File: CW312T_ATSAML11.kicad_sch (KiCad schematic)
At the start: 12 parts, among them P1 PCIEx4 EDGE CONNECTOR, U1 ATSMAL11E16A-AU

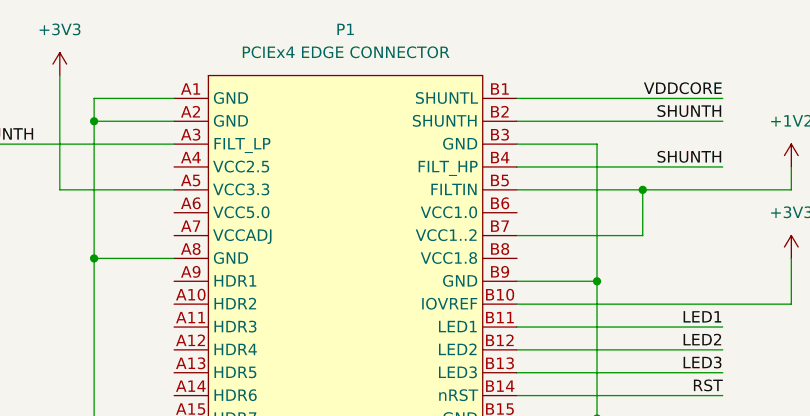
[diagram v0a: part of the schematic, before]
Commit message: updated pcb based off feedback
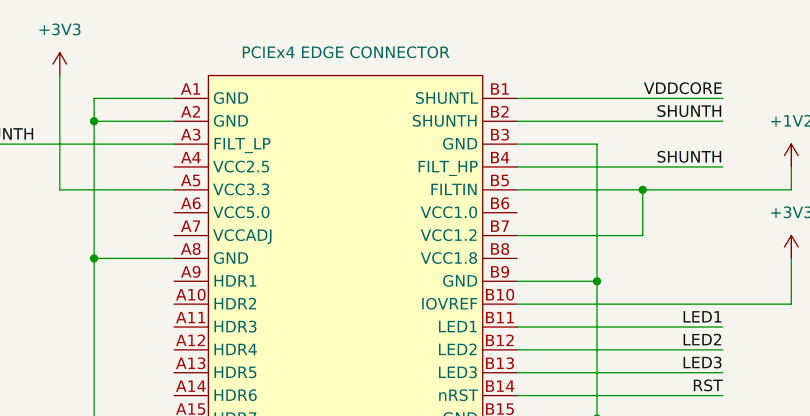
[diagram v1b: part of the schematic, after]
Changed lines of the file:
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@@
 					(size 1.27 1.27)
 				)
+				(hide yes)
 			)
 		)

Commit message: updated ATSAML11 design - Ready for Review
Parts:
- added PCB1: CE, Silkscrren_Symbols:CE-Logo_8.5x6mm_SilkScreen, symbol Silkscreen_Symbols:CE_Free
- added PCB2: Pb_Free, Silkscrren_Symbols:Pb_Free_8.0x8.0mm_SilkScreen, symbol Silkscreen_Symbols:Pb_Free
- added PCB3: WEEE, Silkscrren_Symbols:WEEE-Logo_5.6x8mm_SilkScreen, symbol Silkscreen_Symbols:WEEE
- renumbered C7 to C5, C8 to C6, C5 to C7
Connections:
- no-connect marks 0 -> 46

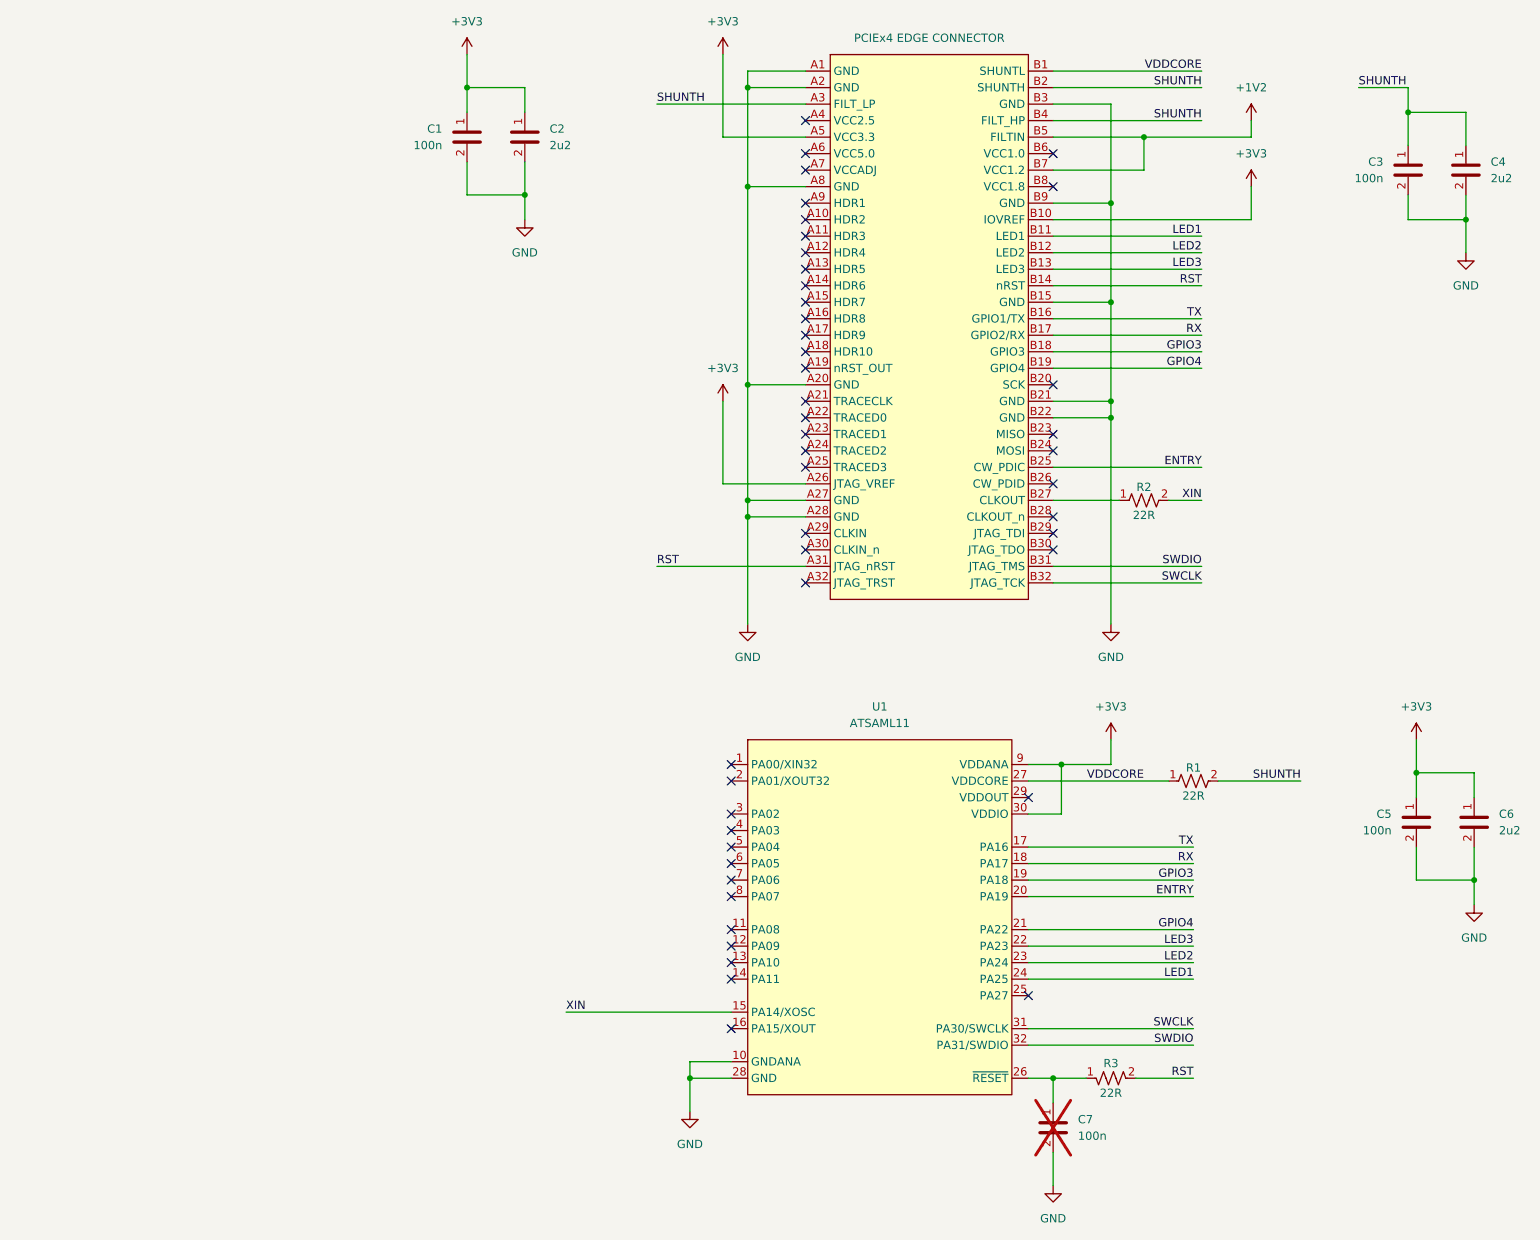
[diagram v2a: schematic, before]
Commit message: updated design -removed pin numbers from passives, updated cap placement, updated silkscreen
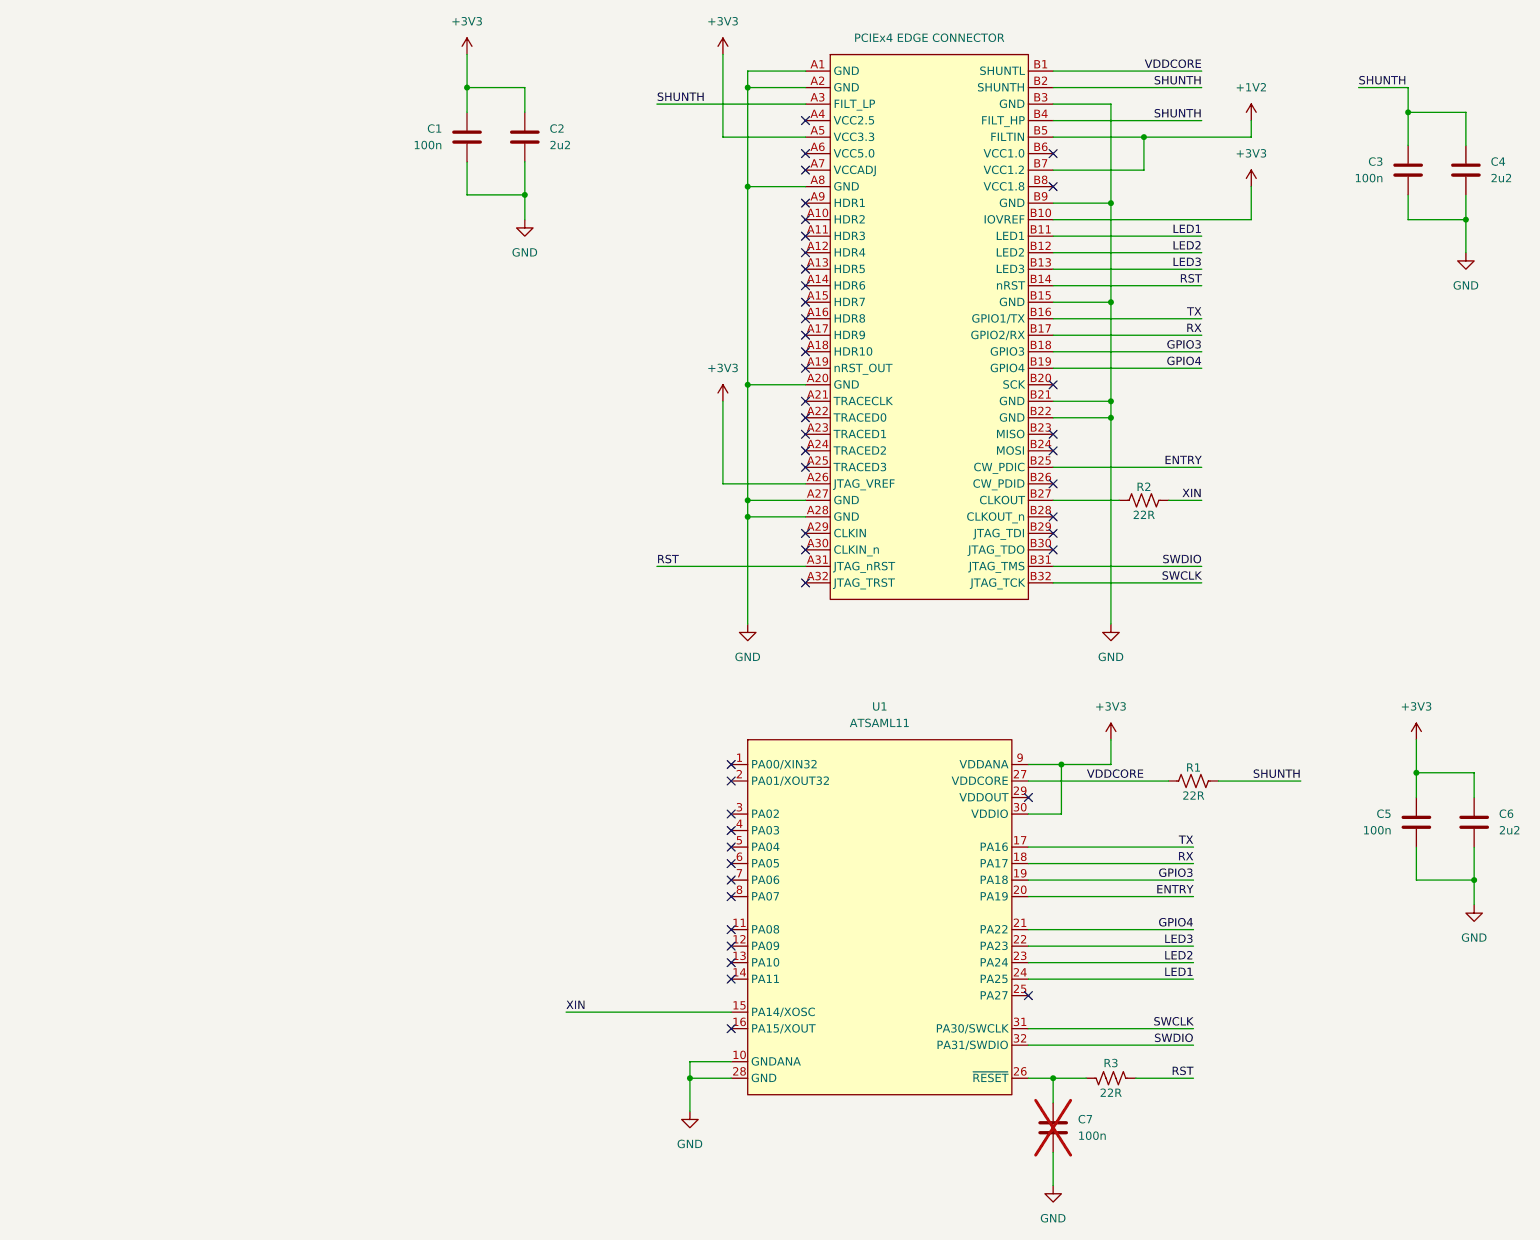
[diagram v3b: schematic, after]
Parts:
- added PCB4: UKCA symbol, Silkscrren_Symbols:UKCA-Logo_8x8mm_SilkScreen, symbol Silkscreen_Symbols:UKCA
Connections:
- net +3V3: now also C1., C2., C5., C6.; no longer C1.1, C2.1, C5.1, C6.1
- net GND: now also C1., C2., C3., C4., C5., C6., C7.; no longer C1.2, C2.2, C3.2, C4.2, C5.2, C6.2, C7.2
- net RST: now also R3.; no longer R3.2
- net SHUNTH: now also C3., C4., R1.; no longer C3.1, C4.1, R1.2
- net VDDCORE: now also R1.; no longer R1.1
- net XIN: now also R2.; no longer R2.2
- net at P1.B27 (CLKOUT): now also R2.; no longer R2.1
- new net: C7., R3., U1.26 (~{RESET})
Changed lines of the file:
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@@
 	)
 	(symbol
+		(lib_name "tutorial_2_library:CAP_100n_50V_0603")
 		(lib_id "tutorial_2_library:CAP_100n_50V_0603")
 		(at 181.61 140.97 90)
@@
 			)
 		)
-		(pin "2"
-		)
-		(pin "1"
+		(pin ""
+		)
+		(pin ""
 		)
 		(instances
@@
 	)
 	(symbol
+		(lib_name "tutorial_2_library:CAP_100n_50V_0603")
 		(lib_id "tutorial_2_library:CAP_100n_50V_0603")
 		(at 35.56 35.56 90)
@@
 			)
 		)
-		(pin "2"
-		)
-		(pin "1"
+		(pin ""
+		)
+		(pin ""
 		)
 		(instances
@@
 	)
 	(symbol
+		(lib_name "tutorial_2_library:RES_22R_0603")
 		(lib_id "tutorial_2_library:RES_22R_0603")
 		(at 134.62 180.34 0)
@@
 			)
 		)
-		(pin "1"
-		)
-		(pin "2"
+		(pin ""
+		)
+		(pin ""
 		)
 		(instances
@@
 	)
 	(symbol
+		(lib_name "tutorial_2_library:CAP_2u2_16V_0603")
 		(lib_id "tutorial_2_library:CAP_2u2_16V_0603")
 		(at 189.23 40.64 270)
@@
 			)
 		)
-		(pin "2"
-		)
-		(pin "1"
+		(pin ""
+		)
+		(pin ""
 		)
 		(instances
@@
 	)
 	(symbol
+		(lib_id "Silkscreen_Symbols:UKCA")
+		(at -16.51 193.04 0)
+		(unit 1)
+		(exclude_from_sim no)
+		(in_bom yes)
+		(on_board yes)
+		(dnp no)
+		(fields_autoplaced yes)
+		(property "Reference" "PCB4"
+			(at -13.97 191.7699 0)
+			(effects
+				(font
+					(size 1.27 1.27)
+				)
+				(justify left)
+				(hide yes)
+			)
+		)
+		(property "Value" "UKCA symbol"
+			(at -13.97 193.0399 0)
+			(effects
+				(font
+					(size 1.27 1.27)
+				)
+				(justify left)
+				(hide yes)
+			)
+		)
+		(property "Footprint" "Silkscrren_Symbols:UKCA-Logo_8x8mm_SilkScreen"
+			(at -16.51 193.04 0)
+			(effects
+				(font
+					(size 1.27 1.27)
+				)
+				(hide yes)
+			)
+		)
+		(property "Datasheet" ""
+			(at -16.51 193.04 0)
+			(effects
+				(font
+					(size 1.27 1.27)
+				)
+				(hide yes)
+			)
+		)
+		(property "Description" ""
+			(at -16.51 193.04 0)
+			(effects
+				(font
+					(size 1.27 1.27)
+				)
+				(hide yes)
+			)
+		)
+		(instances
+			(project ""
+				(path "/497ddeb2-6500-4436-ac31-e3cfdb79cc3f"
+					(reference "PCB4")
+					(unit 1)
+				)
+			)
+		)
+	)
+	(symbol
 		(lib_id "power:GND")
 		(at 189.23 53.34 0)
@@
 	)
 	(symbol
+		(lib_name "tutorial_2_library:CAP_2u2_16V_0603")
 		(lib_id "tutorial_2_library:CAP_2u2_16V_0603")
 		(at 190.5 140.97 270)
@@
 			)
 		)
-		(pin "2"
-		)
-		(pin "1"
+		(pin ""
+		)
+		(pin ""
 		)
 		(instances
@@
 	)
 	(symbol
+		(lib_name "tutorial_2_library:CAP_2u2_16V_0603")
 		(lib_id "tutorial_2_library:CAP_2u2_16V_0603")
 		(at 44.45 35.56 270)
@@
 			)
 		)
-		(pin "2"
-		)
-		(pin "1"
+		(pin ""
+		)
+		(pin ""
 		)
 		(instances
@@
 	)
 	(symbol
+		(lib_name "tutorial_2_library:RES_22R_0603")
 		(lib_id "tutorial_2_library:RES_22R_0603")
 		(at 139.7 91.44 0)
@@
 			)
 		)
-		(pin "1"
-		)
-		(pin "2"
+		(pin ""
+		)
+		(pin ""
 		)
 		(instances
@@
 	)
 	(symbol
+		(lib_name "tutorial_2_library:CAP_100n_50V_0603")
 		(lib_id "tutorial_2_library:CAP_100n_50V_0603")
 		(at 180.34 40.64 90)
@@
 			)
 		)
-		(pin "2"
-		)
-		(pin "1"
+		(pin ""
+		)
+		(pin ""
 		)
 		(instances
@@
 	)
 	(symbol
+		(lib_name "tutorial_2_library:RES_22R_0603")
 		(lib_id "tutorial_2_library:RES_22R_0603")
 		(at 147.32 134.62 0)
@@
 			)
 		)
-		(pin "1"
-		)
-		(pin "2"
+		(pin ""
+		)
+		(pin ""
 		)
 		(instances
@@
 	)
 	(symbol
+		(lib_name "tutorial_2_library:CAP_100n_50V_0603")
 		(lib_id "tutorial_2_library:CAP_100n_50V_0603")
 		(at 125.73 187.96 270)
@@
 			)
 		)
-		(pin "2"
-		)
-		(pin "1"
-		)
-		(instances
+		(pin ""
+		)
+		(pin ""
+		)
+		(instances

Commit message: Changed how pins were hidden to ensure the nets remain
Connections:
- net +3V3: now also C1.1, C2.1, C5.1, C6.1; no longer C1., C2., C5., C6.
- net GND: now also C1.2, C2.2, C3.2, C4.2, C5.2, C6.2, C7.2; no longer C1., C2., C3., C4., C5., C6., C7.
- net RST: now also R3.2; no longer R3.
- net SHUNTH: now also C3.1, C4.1, R1.2; no longer C3., C4., R1.
- net VDDCORE: now also R1.1; no longer R1.
- net XIN: now also R2.2; no longer R2.
- net at P1.B27 (CLKOUT): now also R2.1; no longer R2.
- new net: C7.1, R3.1, U1.26 (~{RESET})
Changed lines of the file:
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@@
 	)
 	(symbol
-		(lib_name "tutorial_2_library:CAP_100n_50V_0603")
 		(lib_id "tutorial_2_library:CAP_100n_50V_0603")
 		(at 181.61 140.97 90)
@@
 			)
 		)
-		(pin ""
-		)
-		(pin ""
+		(pin "2"
+		)
+		(pin "1"
 		)
 		(instances
@@
 	)
 	(symbol
-		(lib_name "tutorial_2_library:CAP_100n_50V_0603")
 		(lib_id "tutorial_2_library:CAP_100n_50V_0603")
 		(at 35.56 35.56 90)
@@
 			)
 		)
-		(pin ""
-		)
-		(pin ""
+		(pin "1"
+		)
+		(pin "2"
 		)
 		(instances
@@
 	)
 	(symbol
-		(lib_name "tutorial_2_library:RES_22R_0603")
 		(lib_id "tutorial_2_library:RES_22R_0603")
 		(at 134.62 180.34 0)
@@
 			)
 		)
-		(pin ""
-		)
-		(pin ""
+		(pin "1"
+		)
+		(pin "2"
 		)
 		(instances
@@
 	)
 	(symbol
-		(lib_name "tutorial_2_library:CAP_2u2_16V_0603")
 		(lib_id "tutorial_2_library:CAP_2u2_16V_0603")
 		(at 189.23 40.64 270)
@@
 			)
 		)
-		(pin ""
-		)
-		(pin ""
+		(pin "1"
+		)
+		(pin "2"
 		)
 		(instances
@@
 	)
 	(symbol
-		(lib_name "tutorial_2_library:CAP_2u2_16V_0603")
 		(lib_id "tutorial_2_library:CAP_2u2_16V_0603")
 		(at 190.5 140.97 270)
@@
 			)
 		)
-		(pin ""
-		)
-		(pin ""
+		(pin "1"
+		)
+		(pin "2"
 		)
 		(instances
@@
 	)
 	(symbol
-		(lib_name "tutorial_2_library:CAP_2u2_16V_0603")
 		(lib_id "tutorial_2_library:CAP_2u2_16V_0603")
 		(at 44.45 35.56 270)
@@
 			)
 		)
-		(pin ""
-		)
-		(pin ""
+		(pin "2"
+		)
+		(pin "1"
 		)
 		(instances
@@
 	)
 	(symbol
-		(lib_name "tutorial_2_library:RES_22R_0603")
 		(lib_id "tutorial_2_library:RES_22R_0603")
 		(at 139.7 91.44 0)
@@
 			)
 		)
-		(pin ""
-		)
-		(pin ""
+		(pin "1"
+		)
+		(pin "2"
 		)
 		(instances
@@
 	)
 	(symbol
-		(lib_name "tutorial_2_library:CAP_100n_50V_0603")
 		(lib_id "tutorial_2_library:CAP_100n_50V_0603")
 		(at 180.34 40.64 90)
@@
 			)
 		)
-		(pin ""
-		)
-		(pin ""
+		(pin "2"
+		)
+		(pin "1"
 		)
 		(instances
@@
 	)
 	(symbol
-		(lib_name "tutorial_2_library:RES_22R_0603")
 		(lib_id "tutorial_2_library:RES_22R_0603")
 		(at 147.32 134.62 0)
@@
 			)
 		)
-		(pin ""
-		)
-		(pin ""
+		(pin "2"
+		)
+		(pin "1"
 		)
 		(instances
@@
 	)
 	(symbol
-		(lib_name "tutorial_2_library:CAP_100n_50V_0603")
 		(lib_id "tutorial_2_library:CAP_100n_50V_0603")
 		(at 125.73 187.96 270)
@@
 			)
 		)
-		(pin ""
-		)
-		(pin ""
-		)
-		(instances
+		(pin "1"
+		)
+		(pin "2"
+		)
+		(instances
